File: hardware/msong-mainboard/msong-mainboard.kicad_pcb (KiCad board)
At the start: 2 copper layers, 1 part

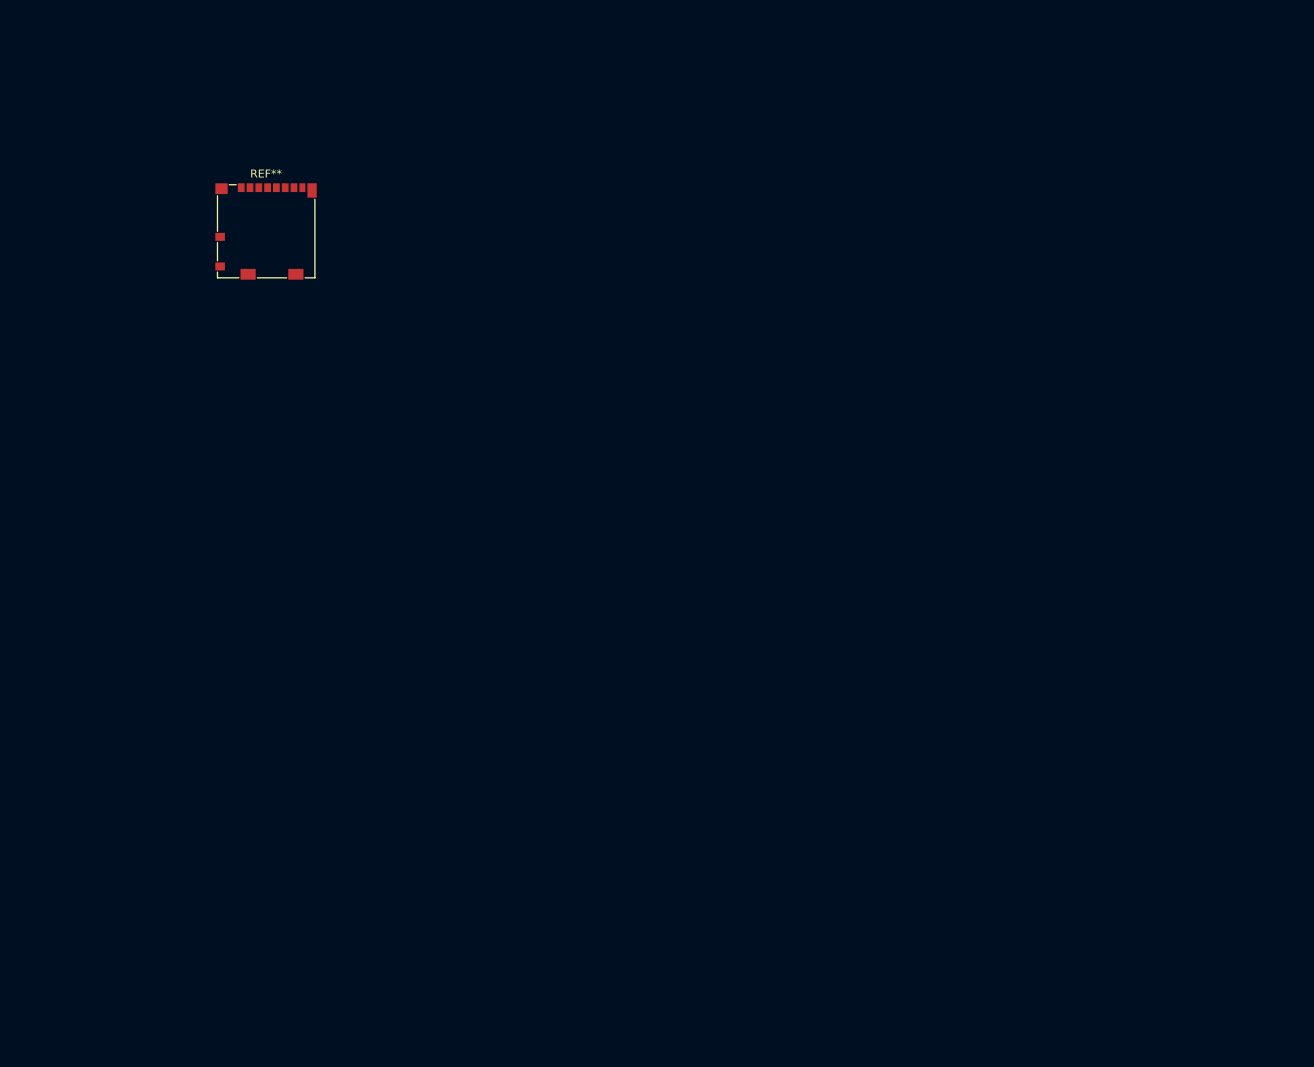
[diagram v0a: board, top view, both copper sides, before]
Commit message: Add basic pcb design (USB-C power ----> RPI Pico)
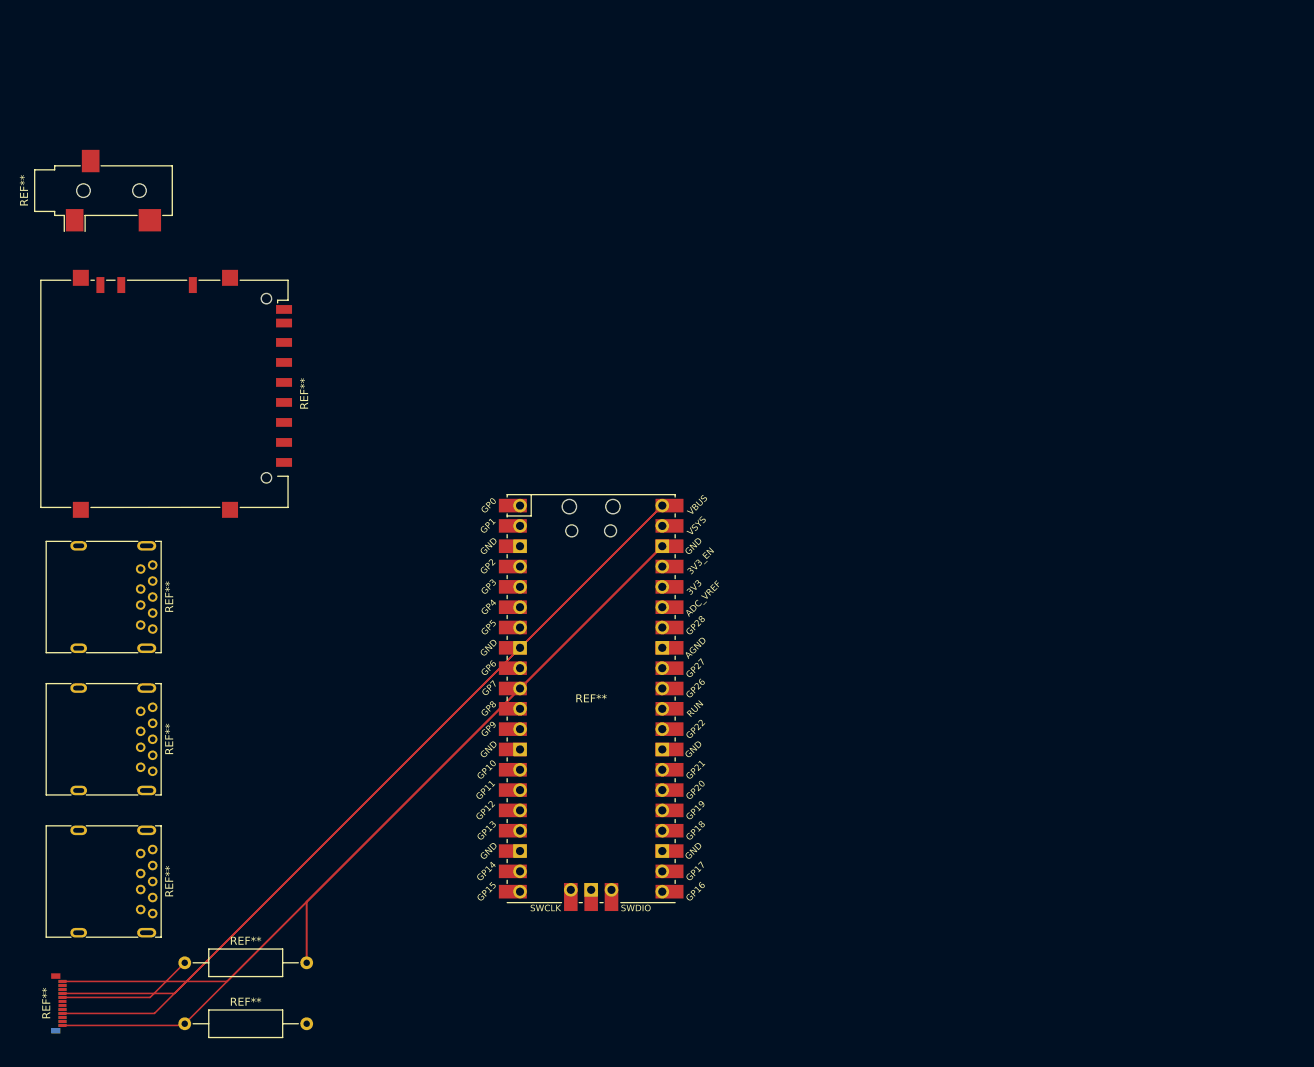
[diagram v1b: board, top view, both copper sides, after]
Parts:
- removed the REF** at (40.6, 43.2)
- added REF**: R_Axial_DIN0309_L9.0mm_D3.2mm_P15.24mm_Horizontal, Resistor_THT:R_Axial_DIN0309_L9.0mm_D3.2mm_P15.24mm_Horizontal, F.Cu at (30.5, 134.6)
- added REF**: Jack_3.5mm_CUI_SJ-3523-SMT_Horizontal, Connector_Audio:Jack_3.5mm_CUI_SJ-3523-SMT_Horizontal, F.Cu at (20.3, 38.1)
- added REF**: RPi_Pico_SMD_TH, MCU_RaspberryPi_and_Boards:RPi_Pico_SMD_TH, F.Cu at (81.3, 101.6)
- added REF**: USB3_A_Molex_48393-001, Connector_USB:USB3_A_Molex_48393-001, F.Cu at (25.0, 121.0)
- added REF**: R_Axial_DIN0309_L9.0mm_D3.2mm_P15.24mm_Horizontal, Resistor_THT:R_Axial_DIN0309_L9.0mm_D3.2mm_P15.24mm_Horizontal, F.Cu at (30.5, 142.2)
- added REF**: USB_C_Plug_Molex_105444, Connector_USB:USB_C_Plug_Molex_105444, F.Cu at (15.2, 139.7)
- added REF**: USB3_A_Molex_48393-001, Connector_USB:USB3_A_Molex_48393-001, F.Cu at (25.0, 103.2)
- added REF**: USB3_A_Molex_48393-001, Connector_USB:USB3_A_Molex_48393-001, F.Cu at (25.0, 85.4)
- added REF**: SD_Hirose_DM1AA_SF_PEJ82, Connector_Card:SD_Hirose_DM1AA_SF_PEJ82, F.Cu at (27.9, 63.5)
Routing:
- net (no net): track 0.00 -> 486.3 mm

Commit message: Add some tuff
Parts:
- removed the REF** at (30.5, 134.6)
- removed the REF** at (30.5, 142.2)
- added ?: , , F.Cu at (35.6, 139.7)
- added ?: , , F.Cu at (35.6, 137.2)
- added REF**: LED_D3.0mm_Clear, LED_THT:LED_D3.0mm_Clear, F.Cu at (20.3, 20.3)
- added REF**: LCD-016N002L, Display:LCD-016N002L, F.Cu at (128.0, 66.8)
- added REF**: R_0201_0603Metric, Resistor_SMD:R_0201_0603Metric, F.Cu at (20.3, 142.2)
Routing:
- net (no net): track 486.3 -> 1302.3 mm
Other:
- board text added: "Bat+"
- board text added: "Bat-"
- board text added: "Power"
